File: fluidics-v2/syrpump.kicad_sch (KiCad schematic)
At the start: 7 parts, among them U9 MAX3221

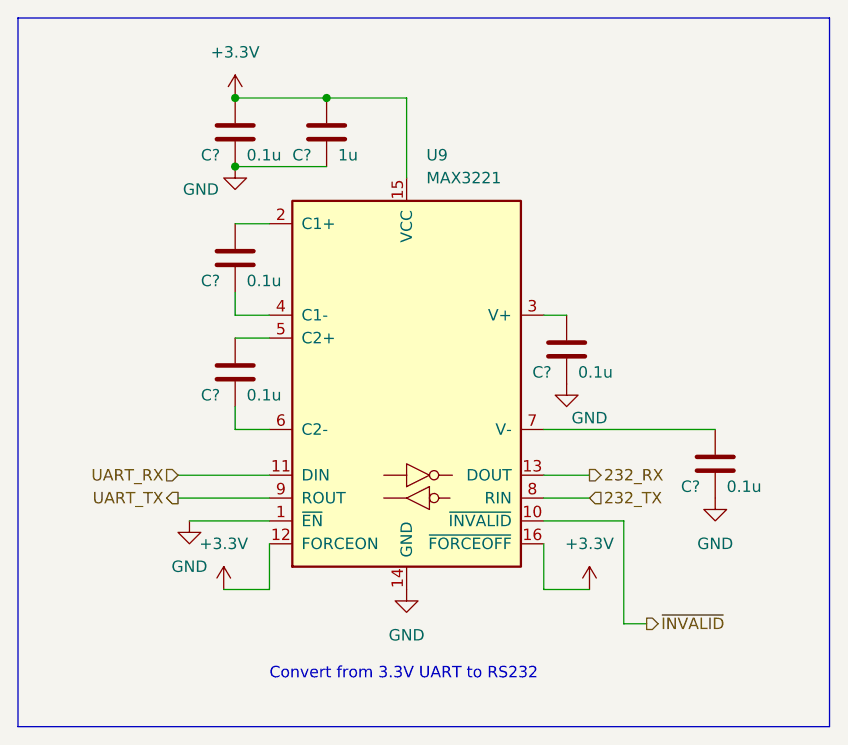
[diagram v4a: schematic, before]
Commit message: added new connector for motor control daughter board. began layout
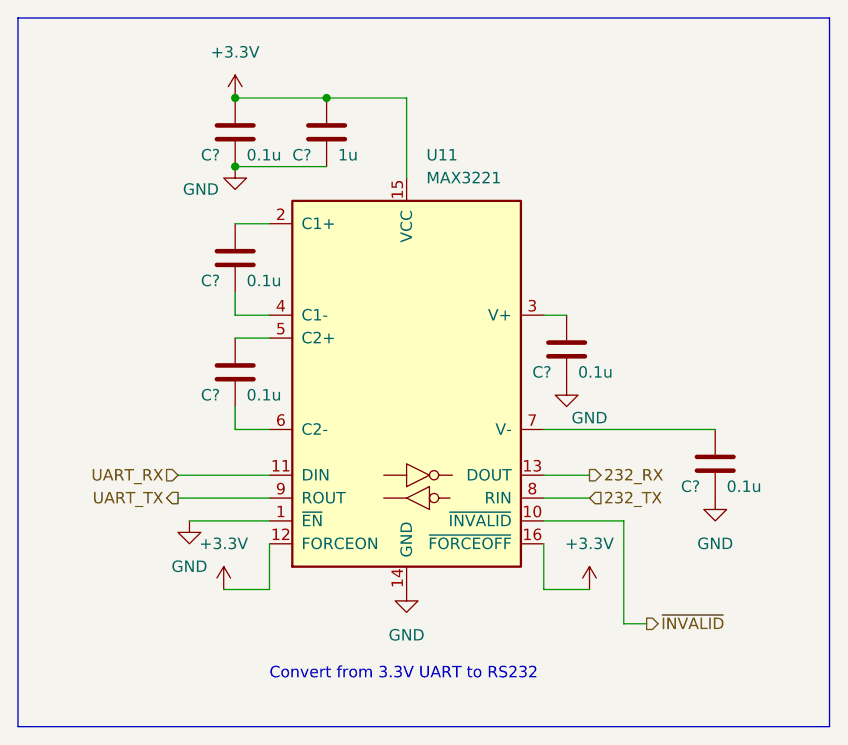
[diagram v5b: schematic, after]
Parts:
- renumbered U9 to U11
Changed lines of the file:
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@@
         )
         (path "/0ec91c42-8aad-437d-8c85-5e10f0e51fe0/40e657d1-9450-4917-aa0c-637ab5e93f67"
-          (reference "C13") (unit 1)
+          (reference "C15") (unit 1)
         )
       )
@@
   (symbol (lib_id "power:+3.3V") (at 123.19 85.09 0) (unit 1)
     (in_bom yes) (on_board yes) (dnp no) (fields_autoplaced)
-    (property "Reference" "#PWR0122" (at 123.19 88.9 0)
+    (property "Reference" "#PWR0145" (at 123.19 88.9 0)
       (effects (font (size 1.27 1.27)) hide)
     )
@@
       (project "fluidics-v2"
         (path "/0ec91c42-8aad-437d-8c85-5e10f0e51fe0/40e657d1-9450-4917-aa0c-637ab5e93f67"
-          (reference "#PWR0122") (unit 1)
+          (reference "#PWR0145") (unit 1)
         )
       )
@@
   (symbol (lib_id "power:GND") (at 137.16 74.93 0) (unit 1)
     (in_bom yes) (on_board yes) (dnp no) (fields_autoplaced)
-    (property "Reference" "#PWR0123" (at 137.16 81.28 0)
+    (property "Reference" "#PWR0146" (at 137.16 81.28 0)
       (effects (font (size 1.27 1.27)) hide)
     )
@@
       (project "fluidics-v2"
         (path "/0ec91c42-8aad-437d-8c85-5e10f0e51fe0/40e657d1-9450-4917-aa0c-637ab5e93f67"
-          (reference "#PWR0123") (unit 1)
+          (reference "#PWR0146") (unit 1)
         )
       )
@@
         )
         (path "/0ec91c42-8aad-437d-8c85-5e10f0e51fe0/40e657d1-9450-4917-aa0c-637ab5e93f67"
-          (reference "C17") (unit 1)
+          (reference "C19") (unit 1)
         )
       )
@@
         )
         (path "/0ec91c42-8aad-437d-8c85-5e10f0e51fe0/40e657d1-9450-4917-aa0c-637ab5e93f67"
+          (reference "C18") (unit 1)
+        )
+      )
+    )
+  )
+  (symbol (lib_id "power:GND") (at 83.82 38.1 0) (unit 1)
+    (in_bom yes) (on_board yes) (dnp no)
+    (property "Reference" "#PWR0142" (at 83.82 44.45 0)
+      (effects (font (size 1.27 1.27)) hide)
+    )
+    (property "Value" "GND" (at 80.01 40.64 0)
+      (effects (font (size 1.27 1.27)))
+    )
+    (property "Footprint" "" (at 83.82 38.1 0)
+      (effects (font (size 1.27 1.27)) hide)
+    )
+    (property "Datasheet" "" (at 83.82 38.1 0)
+      (effects (font (size 1.27 1.27)) hide)
+    )
+    (pin "1")
+    (instances
+      (project "fluidics-v2"
+        (path "/0ec91c42-8aad-437d-8c85-5e10f0e51fe0/40e657d1-9450-4917-aa0c-637ab5e93f67"
+          (reference "#PWR0142") (unit 1)
+        )
+      )
+    )
+  )
+  (symbol (lib_id "Device:C") (at 83.82 48.26 0) (unit 1)
+    (in_bom yes) (on_board yes) (dnp no)
+    (property "Reference" "C?" (at 80.01 50.8 0)
+      (effects (font (size 1.27 1.27)) (justify left))
+    )
+    (property "Value" "0.1u" (at 85.09 50.8 0)
+      (effects (font (size 1.27 1.27)) (justify left))
+    )
+    (property "Footprint" "Capacitor_SMD:C_0603_1608Metric" (at 84.7852 52.07 0)
+      (effects (font (size 1.27 1.27)) hide)
+    )
+    (property "Datasheet" "~" (at 83.82 48.26 0)
+      (effects (font (size 1.27 1.27)) hide)
+    )
+    (pin "1")
+    (pin "2")
+    (instances
+      (project "fluidics-v2"
+        (path "/0ec91c42-8aad-437d-8c85-5e10f0e51fe0/c1c30de3-a3db-48df-8d6b-b2f91b9251f0"
+          (reference "C?") (unit 1)
+        )
+        (path "/0ec91c42-8aad-437d-8c85-5e10f0e51fe0/40e657d1-9450-4917-aa0c-637ab5e93f67"
           (reference "C16") (unit 1)
         )
@@
     )
   )
-  (symbol (lib_id "power:GND") (at 83.82 38.1 0) (unit 1)
-    (in_bom yes) (on_board yes) (dnp no)
-    (property "Reference" "#PWR0119" (at 83.82 44.45 0)
-      (effects (font (size 1.27 1.27)) hide)
-    )
-    (property "Value" "GND" (at 80.01 40.64 0)
-      (effects (font (size 1.27 1.27)))
-    )
-    (property "Footprint" "" (at 83.82 38.1 0)
-      (effects (font (size 1.27 1.27)) hide)
-    )
-    (property "Datasheet" "" (at 83.82 38.1 0)
-      (effects (font (size 1.27 1.27)) hide)
-    )
-    (pin "1")
-    (instances
-      (project "fluidics-v2"
-        (path "/0ec91c42-8aad-437d-8c85-5e10f0e51fe0/40e657d1-9450-4917-aa0c-637ab5e93f67"
-          (reference "#PWR0119") (unit 1)
-        )
-      )
-    )
-  )
-  (symbol (lib_id "Device:C") (at 83.82 48.26 0) (unit 1)
-    (in_bom yes) (on_board yes) (dnp no)
-    (property "Reference" "C?" (at 80.01 50.8 0)
-      (effects (font (size 1.27 1.27)) (justify left))
-    )
-    (property "Value" "0.1u" (at 85.09 50.8 0)
-      (effects (font (size 1.27 1.27)) (justify left))
-    )
-    (property "Footprint" "Capacitor_SMD:C_0603_1608Metric" (at 84.7852 52.07 0)
-      (effects (font (size 1.27 1.27)) hide)
-    )
-    (property "Datasheet" "~" (at 83.82 48.26 0)
-      (effects (font (size 1.27 1.27)) hide)
-    )
-    (pin "1")
-    (pin "2")
-    (instances
-      (project "fluidics-v2"
-        (path "/0ec91c42-8aad-437d-8c85-5e10f0e51fe0/c1c30de3-a3db-48df-8d6b-b2f91b9251f0"
-          (reference "C?") (unit 1)
-        )
-        (path "/0ec91c42-8aad-437d-8c85-5e10f0e51fe0/40e657d1-9450-4917-aa0c-637ab5e93f67"
-          (reference "C14") (unit 1)
-        )
-      )
-    )
-  )
   (symbol (lib_id "power:+3.3V") (at 82.55 85.09 0) (unit 1)
     (in_bom yes) (on_board yes) (dnp no) (fields_autoplaced)
-    (property "Reference" "#PWR0117" (at 82.55 88.9 0)
+    (property "Reference" "#PWR0140" (at 82.55 88.9 0)
       (effects (font (size 1.27 1.27)) hide)
     )
@@
       (project "fluidics-v2"
         (path "/0ec91c42-8aad-437d-8c85-5e10f0e51fe0/40e657d1-9450-4917-aa0c-637ab5e93f67"
-          (reference "#PWR0117") (unit 1)
+          (reference "#PWR0140") (unit 1)
         )
       )
@@
   (symbol (lib_id "power:GND") (at 120.65 62.23 0) (unit 1)
     (in_bom yes) (on_board yes) (dnp no)
-    (property "Reference" "#PWR0121" (at 120.65 68.58 0)
+    (property "Reference" "#PWR0144" (at 120.65 68.58 0)
       (effects (font (size 1.27 1.27)) hide)
     )
@@
       (project "fluidics-v2"
         (path "/0ec91c42-8aad-437d-8c85-5e10f0e51fe0/40e657d1-9450-4917-aa0c-637ab5e93f67"
-          (reference "#PWR0121") (unit 1)
+          (reference "#PWR0144") (unit 1)
         )
       )
@@
   (symbol (lib_id "power:+3.3V") (at 83.82 30.48 0) (unit 1)
     (in_bom yes) (on_board yes) (dnp no) (fields_autoplaced)
-    (property "Reference" "#PWR0118" (at 83.82 34.29 0)
+    (property "Reference" "#PWR0141" (at 83.82 34.29 0)
       (effects (font (size 1.27 1.27)) hide)
     )
@@
       (project "fluidics-v2"
         (path "/0ec91c42-8aad-437d-8c85-5e10f0e51fe0/40e657d1-9450-4917-aa0c-637ab5e93f67"
-          (reference "#PWR0118") (unit 1)
+          (reference "#PWR0141") (unit 1)
         )
       )
@@
         )
         (path "/0ec91c42-8aad-437d-8c85-5e10f0e51fe0/40e657d1-9450-4917-aa0c-637ab5e93f67"
-          (reference "C18") (unit 1)
+          (reference "C20") (unit 1)
         )
       )
@@
   (symbol (lib_id "Interface_UART:MAX3221") (at 102.87 62.23 0) (unit 1)
     (in_bom yes) (on_board yes) (dnp no) (fields_autoplaced)
-    (property "Reference" "U9" (at 105.0641 36.83 0)
+    (property "Reference" "U11" (at 105.0641 36.83 0)
       (effects (font (size 1.27 1.27)) (justify left))
     )
@@
       (project "fluidics-v2"
         (path "/0ec91c42-8aad-437d-8c85-5e10f0e51fe0/40e657d1-9450-4917-aa0c-637ab5e93f67"
-          (reference "U9") (unit 1)
+          (reference "U11") (unit 1)
         )
       )
@@
         )
         (path "/0ec91c42-8aad-437d-8c85-5e10f0e51fe0/40e657d1-9450-4917-aa0c-637ab5e93f67"
-          (reference "C15") (unit 1)
+          (reference "C17") (unit 1)
         )
       )
@@
   (symbol (lib_id "power:GND") (at 78.74 77.47 0) (unit 1)
     (in_bom yes) (on_board yes) (dnp no) (fields_autoplaced)
-    (property "Reference" "#PWR0116" (at 78.74 83.82 0)
+    (property "Reference" "#PWR0139" (at 78.74 83.82 0)
       (effects (font (size 1.27 1.27)) hide)
     )
@@
       (project "fluidics-v2"
         (path "/0ec91c42-8aad-437d-8c85-5e10f0e51fe0/40e657d1-9450-4917-aa0c-637ab5e93f67"
-          (reference "#PWR0116") (unit 1)
+          (reference "#PWR0139") (unit 1)
         )
       )
@@
   (symbol (lib_id "power:GND") (at 102.87 85.09 0) (unit 1)
     (in_bom yes) (on_board yes) (dnp no) (fields_autoplaced)
-    (property "Reference" "#PWR0120" (at 102.87 91.44 0)
+    (property "Reference" "#PWR0143" (at 102.87 91.44 0)
       (effects (font (size 1.27 1.27)) hide)
     )
@@
       (project "fluidics-v2"
         (path "/0ec91c42-8aad-437d-8c85-5e10f0e51fe0/40e657d1-9450-4917-aa0c-637ab5e93f67"
-          (reference "#PWR0120") (unit 1)
-        )
-      )
+          (reference "#PWR0143") (unit 1)
+        )
+      )
